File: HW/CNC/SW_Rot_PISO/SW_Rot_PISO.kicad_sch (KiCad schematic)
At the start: 18 parts, among them J1 1x13 2.54mm male 90deg, J2 1x8 2.54mm female 90deg, J3 1x13 2.54mm male 90deg, J4 1x13 2.54mm male 90deg, U1 74LS166, U2 74LS166

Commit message: Correction.
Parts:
- R1, R10, R11, R12, R2, R3, R4, R5, R6, R7, R8, R9: value 1k -> 10k
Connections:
- net GND: now also U1.6 (CE), U2.6 (CE)
- net VCC: no longer U1.6 (CE), U2.6 (CE)
- net LOAD renamed N_LOAD
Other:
- moved on the sheet: R1, R10, R11, R12, R2, R3, R4, R5, R6, R7, R8, R9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

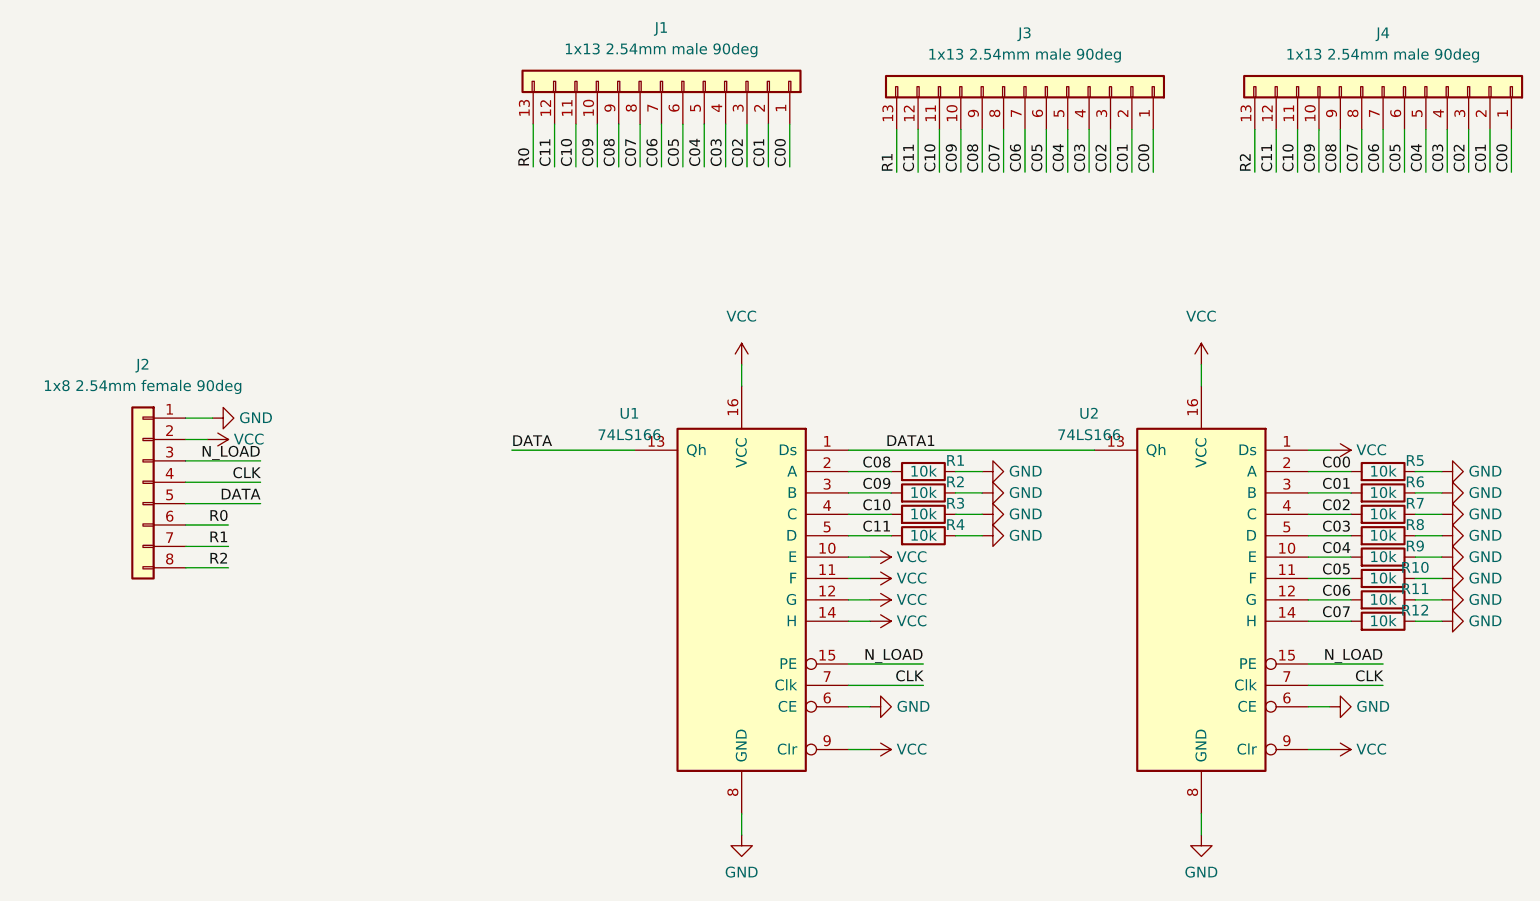
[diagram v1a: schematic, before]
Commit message: Corrections after soldering prototype.
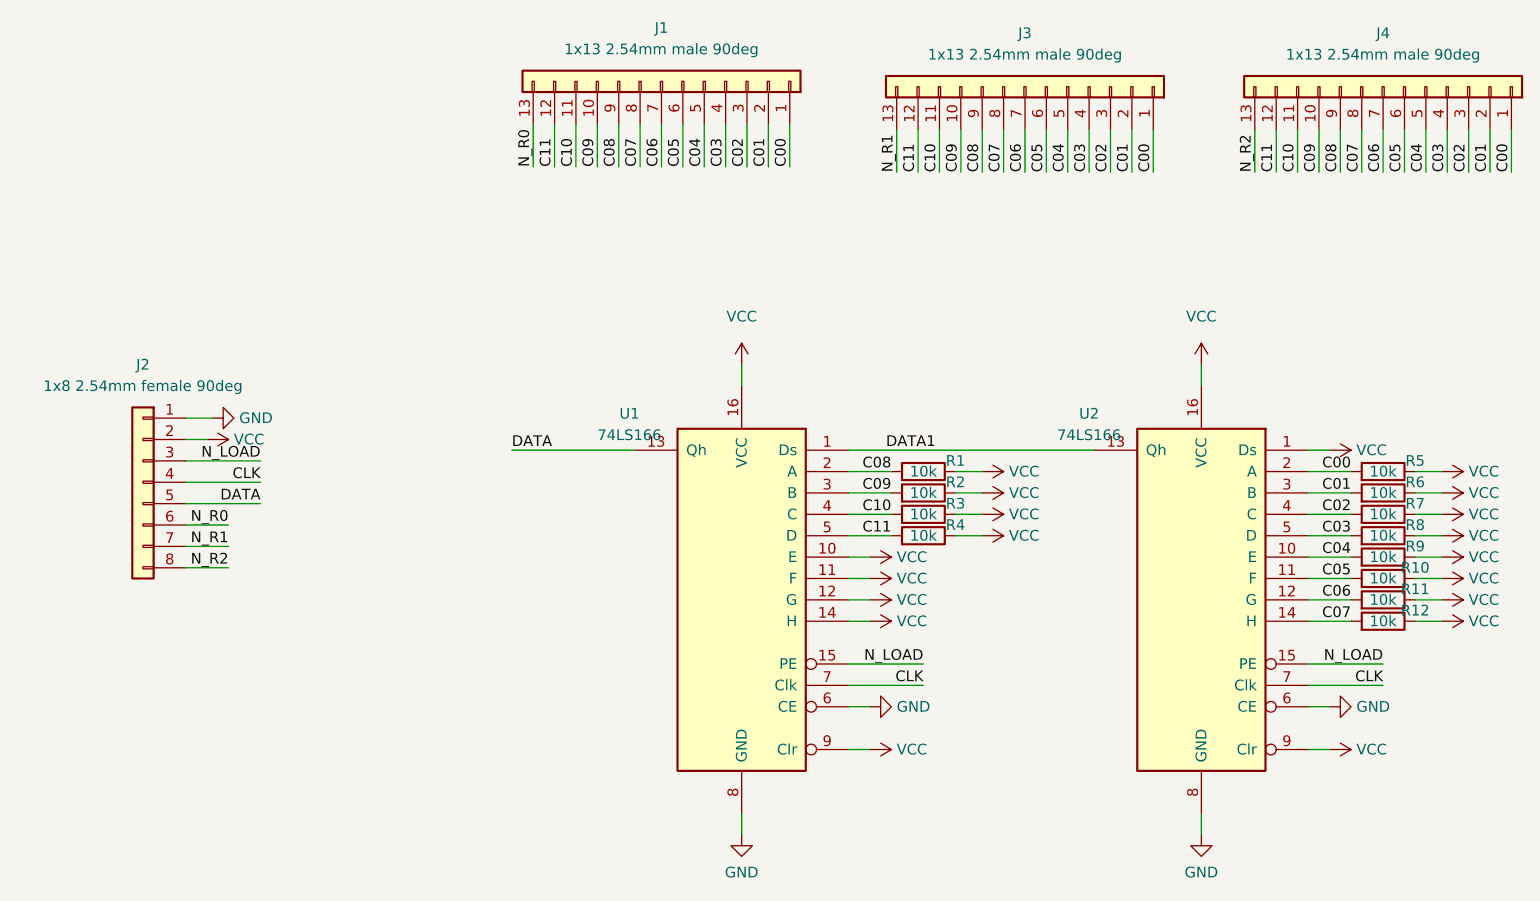
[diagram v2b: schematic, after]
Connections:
- net GND: no longer R1.1, R10.1, R11.1, R12.1, R2.1, R3.1, R4.1, R5.1, R6.1, R7.1, R8.1, R9.1
- net VCC: now also R1.1, R10.1, R11.1, R12.1, R2.1, R3.1, R4.1, R5.1, R6.1, R7.1, R8.1, R9.1
- net R0 renamed N_R0
- net R1 renamed N_R1
- net R2 renamed N_R2
